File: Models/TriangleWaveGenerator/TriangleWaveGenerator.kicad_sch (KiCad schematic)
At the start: 4 parts

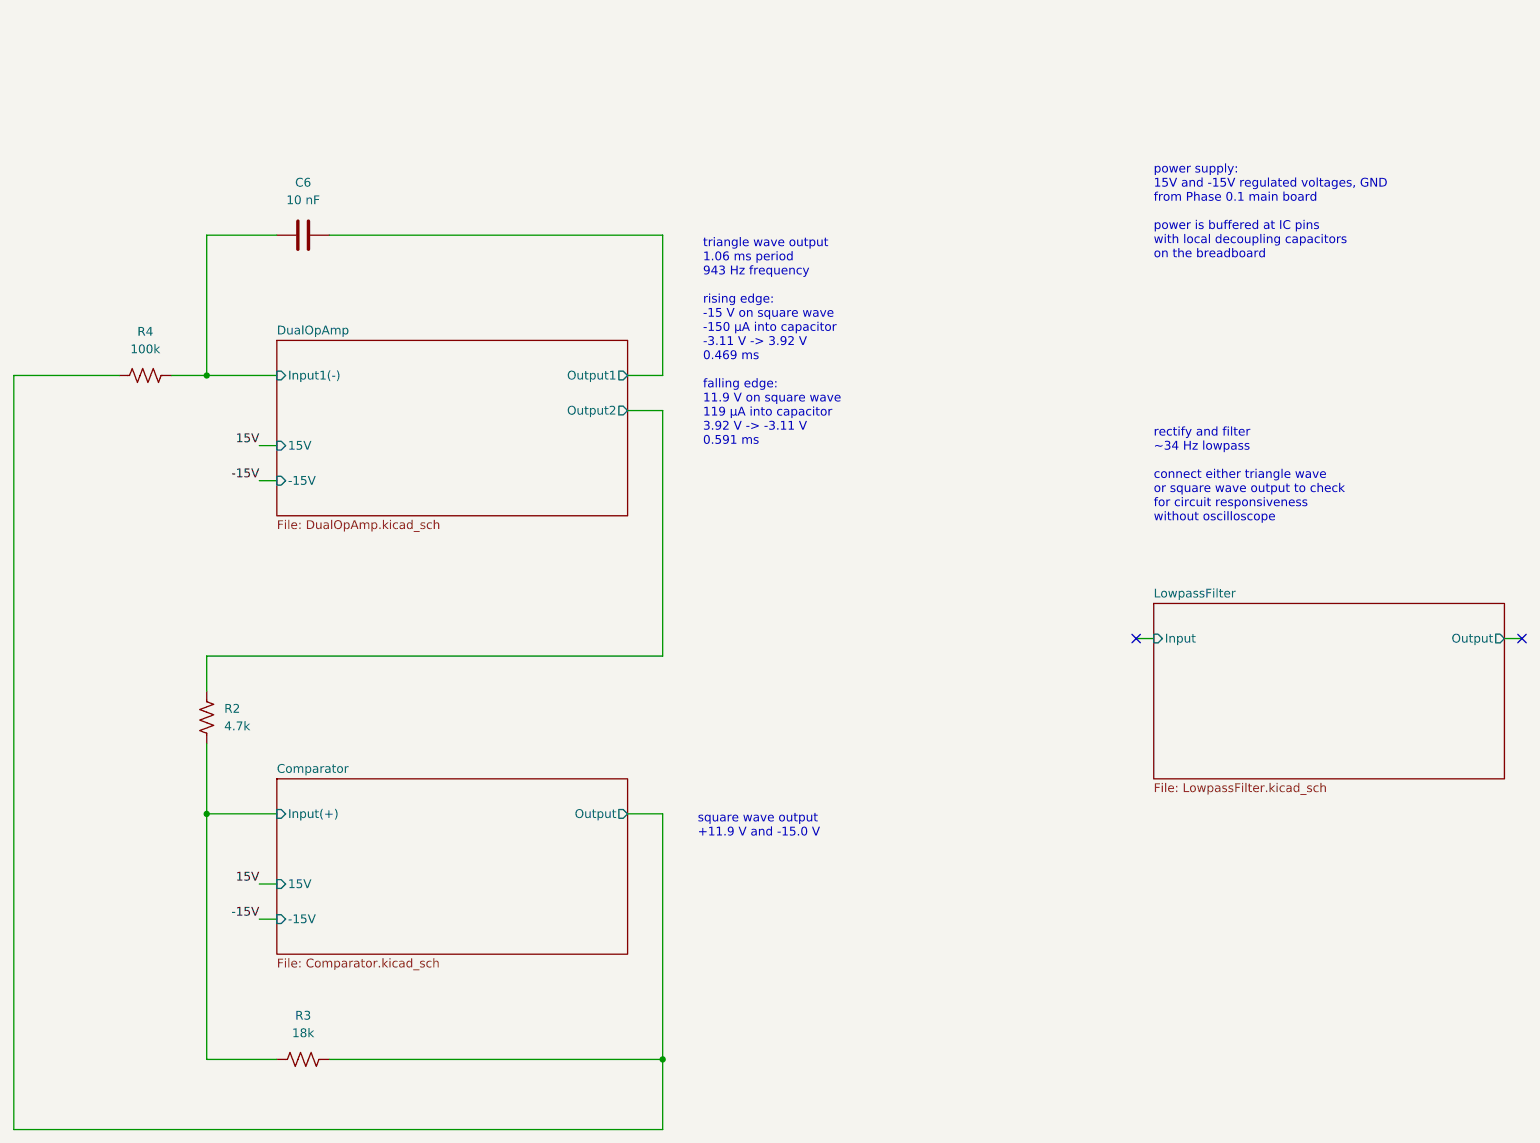
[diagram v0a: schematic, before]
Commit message: Added voltage divider to schematic
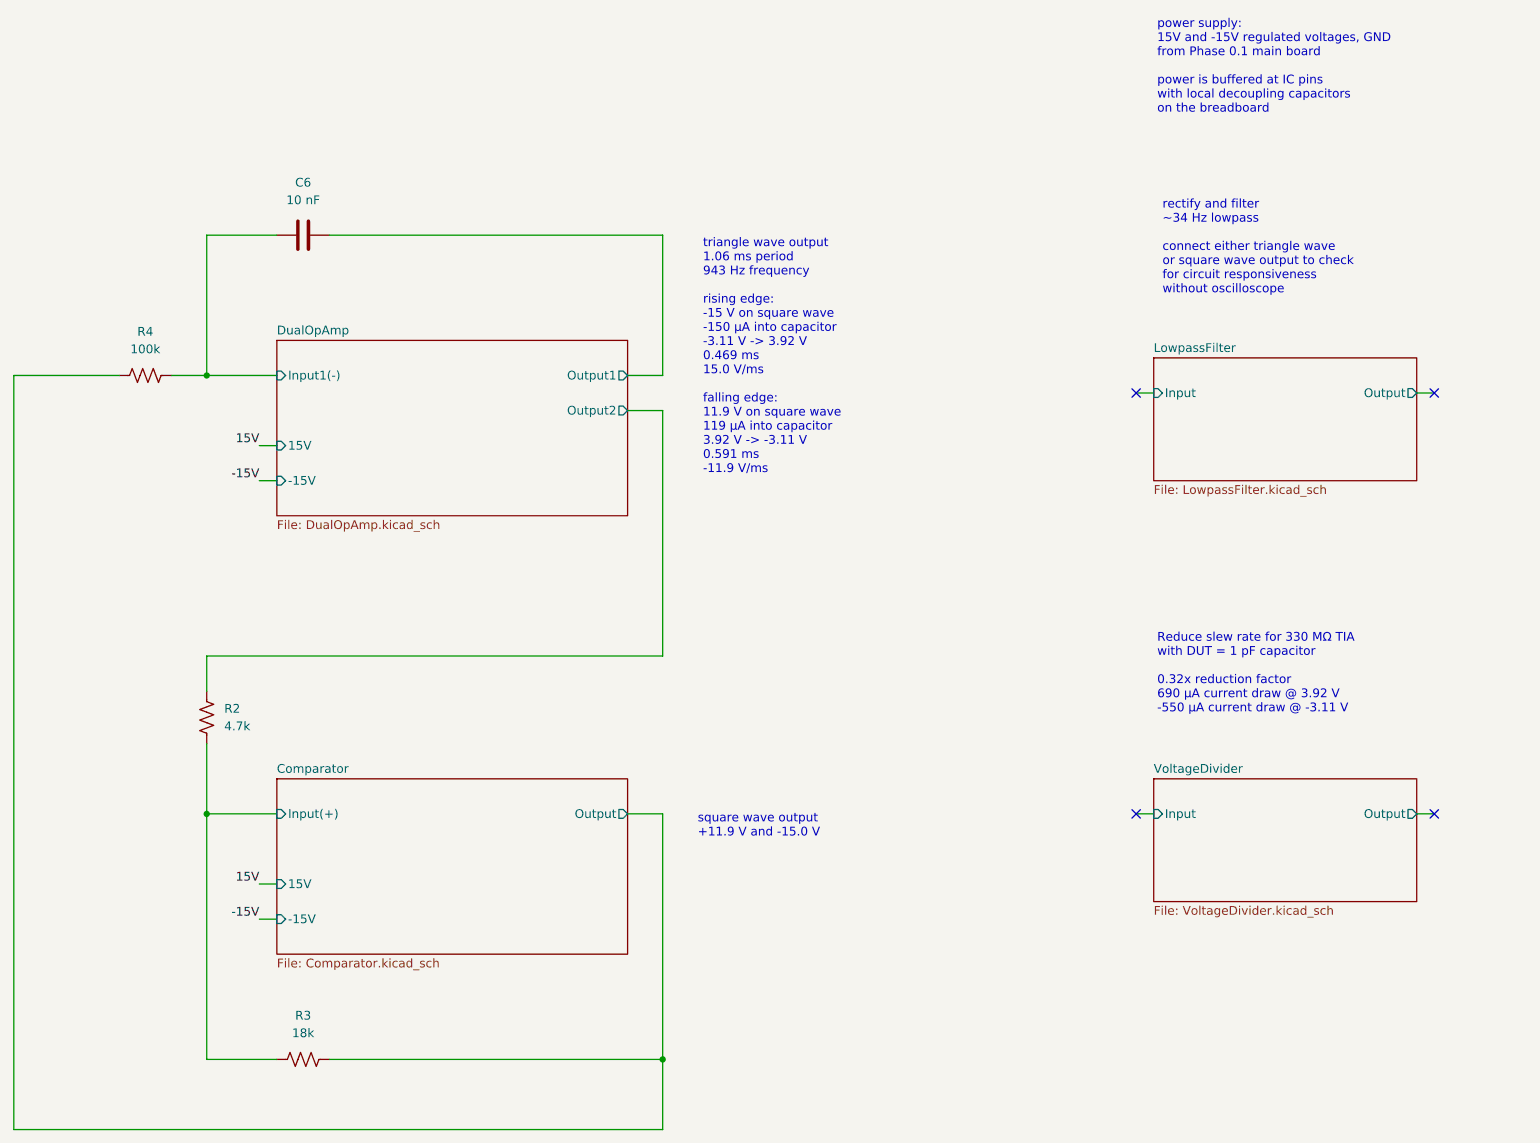
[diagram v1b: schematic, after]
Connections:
- no-connect marks 2 -> 4
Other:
- added sheet VoltageDivider (VoltageDivider.kicad_sch)
- note added: "Reduce slew rate for 330 MΩ TIA with DUT = 1 pF capacitor 0.32x reduction factor 690 μA current draw @ 3.92 V -550 μA current draw @ -3.11 V"
- note added: "triangle wave output 1.06 ms period 943 Hz frequency rising edge: -15 V on square wave -150 μA into capacitor -3.11 V -> 3.92 V 0.469 ms 15.0 V/ms falling edge: 11.9 V on square wave 119 μA into capacitor 3.92 V -> -3.11 V 0.591 ms -11.9 V/ms"
- note removed: "triangle wave output 1.06 ms period 943 Hz frequency rising edge: -15 V on square wave -150 μA into capacitor -3.11 V -> 3.92 V 0.469 ms falling edge: 11.9 V on square wave 119 μA into capacitor 3.92 V -> -3.11 V 0.591 ms"
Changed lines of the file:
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@@
 	(text "power supply:\n15V and -15V regulated voltages, GND\nfrom Phase 0.1 main board\n\npower is buffered at IC pins\nwith local decoupling capacitors\non the breadboard"
 		(exclude_from_sim no)
-		(at 203.2 38.1 0)
+		(at 203.708 17.018 0)
 		(effects
 			(font
@@
 		)
 	)
-	(text "triangle wave output\n1.06 ms period\n943 Hz frequency\n\nrising edge:\n-15 V on square wave\n-150 μA into capacitor\n-3.11 V -> 3.92 V\n0.469 ms\n\nfalling edge:\n11.9 V on square wave\n119 μA into capacitor\n3.92 V -> -3.11 V\n0.591 ms"
+	(text "Reduce slew rate for 330 MΩ TIA\nwith DUT = 1 pF capacitor\n\n0.32x reduction factor\n690 μA current draw @ 3.92 V\n-550 μA current draw @ -3.11 V"
+		(exclude_from_sim no)
+		(at 203.708 105.918 0)
+		(effects
+			(font
+				(size 1.27 1.27)
+			)
+			(justify left top)
+		)
+	)
+	(text "triangle wave output\n1.06 ms period\n943 Hz frequency\n\nrising edge:\n-15 V on square wave\n-150 μA into capacitor\n-3.11 V -> 3.92 V\n0.469 ms\n15.0 V/ms\n\nfalling edge:\n11.9 V on square wave\n119 μA into capacitor\n3.92 V -> -3.11 V\n0.591 ms\n-11.9 V/ms"
 		(exclude_from_sim no)
 		(at 137.922 48.768 0)
@@
 	(text "rectify and filter\n~34 Hz lowpass\n\nconnect either triangle wave\nor square wave output to check\nfor circuit responsiveness\nwithout oscilloscope"
 		(exclude_from_sim no)
-		(at 203.2 76.2 0)
+		(at 204.47 43.18 0)
 		(effects
 			(font
@@
 	)
 	(no_connect
-		(at 256.54 106.68)
+		(at 200.66 132.08)
 	)
 	(no_connect
-		(at 200.66 106.68)
+		(at 243.84 132.08)
+	)
+	(no_connect
+		(at 243.84 71.12)
+	)
+	(no_connect
+		(at 200.66 71.12)
 	)
 	(wire
@@
 	(wire
 		(pts
-			(xy 254 106.68) (xy 256.54 106.68)
+			(xy 241.3 71.12) (xy 243.84 71.12)
 		)
 		(stroke
@@
 	(wire
 		(pts
-			(xy 200.66 106.68) (xy 203.2 106.68)
+			(xy 200.66 71.12) (xy 203.2 71.12)
 		)
 		(stroke
@@
 	(wire
 		(pts
+			(xy 241.3 132.08) (xy 243.84 132.08)
+		)
+		(stroke
+			(width 0)
+			(type default)
+		)
+	)
+	(wire
+		(pts
 			(xy 132.08 177.8) (xy 38.1 177.8)
 		)
@@
 		(pts
 			(xy 66.04 132.08) (xy 66.04 167.64)
+		)
+		(stroke
+			(width 0)
+			(type default)
+		)
+	)
+	(wire
+		(pts
+			(xy 200.66 132.08) (xy 203.2 132.08)
 		)
 		(stroke
@@
 	)
 	(sheet
-		(at 203.2 101.6)
-		(size 50.8 25.4)
+		(at 203.2 66.04)
+		(size 38.1 17.78)
 		(exclude_from_sim no)
 		(in_bom yes)
@@
 		)
 		(property "Sheetname" "LowpassFilter"
-			(at 203.2 100.8884 0)
+			(at 203.2 65.3284 0)
 			(effects
 				(font
@@
 		)
 		(property "Sheetfile" "LowpassFilter.kicad_sch"
-			(at 203.2 127.5846 0)
+			(at 203.2 84.4046 0)
 			(effects
 				(font
@@
 		)
 		(pin "Input" input
-			(at 203.2 106.68 180)
+			(at 203.2 71.12 180)
 			(effects
 				(font
@@
 		)
 		(pin "Output" output
-			(at 254 106.68 0)
+			(at 241.3 71.12 0)
 			(effects
 				(font
@@
 				)
 			)
+		)
+	)
+	(sheet
+		(at 203.2 127)
+		(size 38.1 17.78)
+		(exclude_from_sim no)
+		(in_bom yes)
+		(on_board yes)
+		(dnp no)
+		(fields_autoplaced yes)
+		(stroke
+			(width 0.1524)
+			(type solid)
+		)
+		(fill
+			(color 0 0 0 0.0000)
+		)
+		(property "Sheetname" "VoltageDivider"
+			(at 203.2 126.2884 0)
+			(effects
+				(font
+					(size 1.27 1.27)
+				)
+				(justify left bottom)
+			)
+		)
+		(property "Sheetfile" "VoltageDivider.kicad_sch"
+			(at 203.2 145.3646 0)
+			(effects
+				(font
+					(size 1.27 1.27)
+				)
+				(justify left top)
+			)
+		)
+		(pin "Input" input
+			(at 203.2 132.08 180)
+			(effects
+				(font
+					(size 1.27 1.27)
+				)
+				(justify left)
+			)
+		)
+		(pin "Output" output
+			(at 241.3 132.08 0)
+			(effects
+				(font
+					(size 1.27 1.27)
+				)
+				(justify right)
+			)
+		)
+		(instances
+			(project "TriangleWaveGenerator"
+				(path "/dfa365f3-bdb0-4155-b97b-9be2aee452a3"
+					(page "5")
+				)
+			)
